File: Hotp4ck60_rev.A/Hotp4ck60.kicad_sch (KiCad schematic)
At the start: 53 parts, among them J1 HRO_TYPE-C-31-M-12, SW44 RST, U1 nRF52840, U2 SRV05-4, Y1 32 MHz, Y2 32.768 Khz

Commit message: Fixed path
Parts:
- removed TP1: TestPoint, TestPoint:TestPoint_THTPad_1.0x1.0mm_Drill0.5mm, symbol Connector:TestPoint
- removed TP2, TP3, TP4: TestPoint, TestPoint:TestPoint_THTPad_D1.0mm_Drill0.5mm, symbol Connector:TestPoint
- added J3, J4: Conn_01x04, Connector_PinSocket_2.54mm:PinSocket_1x04_P2.54mm_Vertical, symbol Connector_Generic:Conn_01x04
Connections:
- net +5V: now also U2.5 (VP), J4.1 (Pin_1); no longer U2.2 (VN)
- net Earth: no longer H1.1
- net GND: now also H1.1, R12.2, R13.2, U2.2 (VN), J3.4 (Pin_4), J4.4 (Pin_4); no longer U2.5 (VP)
- net GNDPWR: no longer R12.2, R13.2
- net SWDCLK: now also J3.3 (Pin_3)
- net SWDIO: now also J3.2 (Pin_2)
- net USB-D+: now also J4.3 (Pin_3)
- net USB-D-: now also J4.2 (Pin_2)
- net VDD: now also J3.1 (Pin_1)
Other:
- moved on the sheet: U2

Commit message: Modified PCB designed
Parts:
- removed C14: 100 nF, Capacitor_SMD:C_0402_1005Metric, symbol Device:C_Small
- removed D64: D_TVS, Diode_SMD:D_SOD-123F, symbol Device:D_TVS
- removed L5 (x2): BLM15PX121SN1D, Inductor_SMD:L_0402_1005Metric, symbol Device:L_Small
- removed R13: 1 MOhm, Resistor_SMD:R_0402_1005Metric, symbol Device:R_Small
- added L5: BLM15PX121SN1D, Inductor_SMD:L_0402_1005Metric, symbol Device:L_Small
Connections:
- net Earth is gone; now on net GND: J1.S1 (SHIELD)
- net GNDPWR is gone; now on net GND: J1.A1 (GND), J1.A12 (GND), J1.B1 (GND), J1.B12 (GND)
- net +5V: no longer U2.5 (VP)
- net VBUS: now also U2.5 (VP), L5.1
- net at F1.1: now also L5.2

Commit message: Modified positions
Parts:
- removed L5: BLM15PX121SN1D, Inductor_SMD:L_0402_1005Metric, symbol Device:L_Small
- J3, J4: now left out of the parts list
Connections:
- net +5V: now also U2.5 (VP)
- net USB-D-: now also U2.4 (IO3); no longer U2.1 (IO1)
- net VBUS: now also F1.1; no longer U2.5 (VP)
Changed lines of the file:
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@@
   (junction (at 27.94 57.15) (diameter 0) (color 0 0 0 0)
   )
-  (junction (at 190.5 104.14) (diameter 0) (color 0 0 0 0)
-  )
   (junction (at 135.89 31.75) (diameter 0.9144) (color 0 0 0 0)
   )
@@
   (junction (at 166.37 93.98) (diameter 0) (color 0 0 0 0)
   )
+  (junction (at 190.5 104.14) (diameter 0) (color 0 0 0 0)
+  )
   (junction (at 72.39 167.64) (diameter 0) (color 0 0 0 0)
   )
@@
   (no_connect (at 102.87 125.73))
   (no_connect (at 102.87 59.69))
-  (no_connect (at 203.2 120.65))
+  (no_connect (at 177.8 115.57))
   (no_connect (at 102.87 77.47))
   (no_connect (at 102.87 105.41))
@@
     (stroke (width 0) (type default))
   )
-  (wire (pts (xy 190.5 104.14) (xy 191.77 104.14))
+  (wire (pts (xy 114.3 34.29) (xy 114.3 35.56))
     (stroke (width 0) (type default))
   )
-  (wire (pts (xy 114.3 34.29) (xy 114.3 35.56))
+  (wire (pts (xy 180.34 104.14) (xy 184.15 104.14))
     (stroke (width 0) (type default))
   )
@@
     (stroke (width 0) (type default))
   )
-  (wire (pts (xy 189.23 104.14) (xy 190.5 104.14))
-    (stroke (width 0) (type solid))
-  )
   (wire (pts (xy 182.88 52.07) (xy 182.88 53.34))
     (stroke (width 0) (type solid))
@@
     (stroke (width 0) (type default))
   )
+  (wire (pts (xy 189.23 104.14) (xy 190.5 104.14))
+    (stroke (width 0) (type default))
+  )
   (wire (pts (xy 165.1 83.82) (xy 168.91 83.82))
     (stroke (width 0) (type solid))
@@
     (stroke (width 0) (type default))
   )
-  (wire (pts (xy 205.74 100.33) (xy 205.74 104.14))
+  (wire (pts (xy 196.85 102.87) (xy 196.85 104.14))
     (stroke (width 0) (type default))
   )
-  (wire (pts (xy 205.74 104.14) (xy 204.47 104.14))
+  (wire (pts (xy 190.5 104.14) (xy 196.85 104.14))
     (stroke (width 0) (type default))
   )
@@
     (stroke (width 0) (type default))
   )
-  (wire (pts (xy 196.85 104.14) (xy 199.39 104.14))
-    (stroke (width 0) (type default))
-  )
   (global_label "DEC1" (shape input) (at 203.2 24.13 90) (fields_autoplaced)
     (effects (font (size 1.27 1.27)) (justify left))
@@
     )
   )
-  (global_label "VBUS" (shape input) (at 189.23 104.14 180) (fields_autoplaced)
+  (global_label "VBUS" (shape input) (at 180.34 104.14 180) (fields_autoplaced)
     (effects (font (size 1.27 1.27)) (justify right))
-    (property "Intersheetrefs" "${INTERSHEET_REFS}" (at 181.4256 104.14 0)
+    (property "Intersheetrefs" "${INTERSHEET_REFS}" (at 172.5356 104.14 0)
       (effects (font (size 1.27 1.27)) (justify right) hide)
     )
@@
     )
   )
-  (global_label "USB-D-" (shape bidirectional) (at 177.8 115.57 180) (fields_autoplaced)
-    (effects (font (size 1.27 1.27)) (justify right))
-    (property "Intersheetrefs" "${INTERSHEET_REFS}" (at 165.5581 115.57 0)
-      (effects (font (size 1.27 1.27)) (justify right) hide)
-    )
-  )
   (global_label "col1" (shape output) (at 102.87 151.13 0) (fields_autoplaced)
     (effects (font (size 1.27 1.27)) (justify left))
@@
     )
   )
+  (global_label "USB-D-" (shape bidirectional) (at 203.2 120.65 0) (fields_autoplaced)
+    (effects (font (size 1.27 1.27)) (justify left))
+    (property "Intersheetrefs" "${INTERSHEET_REFS}" (at 215.4419 120.65 0)
+      (effects (font (size 1.27 1.27)) (justify left) hide)
+    )
+  )
   (global_label "row4" (shape input) (at 102.87 62.23 0) (fields_autoplaced)
     (effects (font (size 1.27 1.27)) (justify left))
@@
     )
   )
+  (symbol (lib_id "Device:Fuse_Small") (at 186.69 104.14 0) (unit 1)
+    (in_bom yes) (on_board yes) (dnp no)
+    (property "Reference" "F1" (at 184.15 101.6 0)
+      (effects (font (size 1.27 1.27)))
+    )
+    (property "Value" "750 mA" (at 190.5 101.6 0)
+      (effects (font (size 1.27 1.27)))
+    )
+    (property "Footprint" "Fuse:Fuse_0603_1608Metric" (at 186.69 104.14 0)
+      (effects (font (size 1.27 1.27)) hide)
+    )
+    (property "Datasheet" "~" (at 186.69 104.14 0)
+      (effects (font (size 1.27 1.27)) hide)
+    )
+    (property "LCSC" "C20792" (at 186.69 104.14 0)
+      (effects (font (size 1.27 1.27)) hide)
+    )
+    (pin "1")
+    (pin "2")
+    (instances
+      (project "osprey_rev_a"
+        (path "/86a516b3-939b-48ee-9a25-d0111c577d06/23ee5603-a56a-413f-b0a5-1709895ff4f1"
+          (reference "F1") (unit 1)
+        )
+      )
+      (project "Hotp4ck60"
+        (path "/a57939d7-40ce-4436-8014-db245ef7f3c5"
+          (reference "F1") (unit 1)
+        )
+      )
+      (project "designguide-schematic"
+        (path "/c2a65ddb-3915-4293-98a9-444287fe2a3d"
+          (reference "F1") (unit 1)
+        )
+      )
+    )
+  )
   (symbol (lib_id "power:+5V") (at 199.39 72.39 0) (unit 1)
     (in_bom yes) (on_board yes) (dnp no)
@@
   )
   (symbol (lib_id "Connector_Generic:Conn_01x04") (at 236.22 40.64 0) (unit 1)
-    (in_bom yes) (on_board yes) (dnp no) (fields_autoplaced)
+    (in_bom no) (on_board yes) (dnp no) (fields_autoplaced)
     (property "Reference" "J3" (at 238.76 40.64 0)
       (effects (font (size 1.27 1.27)) (justify left))
@@
     )
   )
-  (symbol (lib_id "Device:Fuse_Small") (at 201.93 104.14 0) (unit 1)
-    (in_bom yes) (on_board yes) (dnp no)
-    (property "Reference" "F1" (at 199.39 101.6 0)
-      (effects (font (size 1.27 1.27)))
-    )
-    (property "Value" "750 mA" (at 205.74 101.6 0)
-      (effects (font (size 1.27 1.27)))
-    )
-    (property "Footprint" "Fuse:Fuse_0603_1608Metric" (at 201.93 104.14 0)
-      (effects (font (size 1.27 1.27)) hide)
-    )
-    (property "Datasheet" "~" (at 201.93 104.14 0)
-      (effects (font (size 1.27 1.27)) hide)
-    )
-    (property "LCSC" "C20792" (at 201.93 104.14 0)
-      (effects (font (size 1.27 1.27)) hide)
-    )
-    (pin "1")
-    (pin "2")
-    (instances
-      (project "osprey_rev_a"
-        (path "/86a516b3-939b-48ee-9a25-d0111c577d06/23ee5603-a56a-413f-b0a5-1709895ff4f1"
-          (reference "F1") (unit 1)
-        )
-      )
-      (project "Hotp4ck60"
-        (path "/a57939d7-40ce-4436-8014-db245ef7f3c5"
-          (reference "F1") (unit 1)
-        )
-      )
-      (project "designguide-schematic"
-        (path "/c2a65ddb-3915-4293-98a9-444287fe2a3d"
-          (reference "F1") (unit 1)
-        )
-      )
-    )
-  )
   (symbol (lib_id "PCM_marbastlib-various:SRV05-4") (at 190.5 118.11 0) (unit 1)
     (in_bom yes) (on_board yes) (dnp no)
@@
     )
   )
-  (symbol (lib_id "Device:L_Small") (at 194.31 104.14 90) (unit 1)
-    (in_bom yes) (on_board yes) (dnp no)
-    (property "Reference" "L5" (at 194.31 101.6 90)
-      (effects (font (size 1.27 1.27)))
-    )
-    (property "Value" "BLM15PX121SN1D" (at 194.31 106.68 90)
-      (effects (font (size 1.27 1.27)))
-    )
-    (property "Footprint" "Inductor_SMD:L_0402_1005Metric" (at 194.31 104.14 0)
-      (effects (font (size 1.27 1.27)) hide)
-    )
-    (property "Datasheet" "~" (at 194.31 104.14 0)
-      (effects (font (size 1.27 1.27)) hide)
-    )
-    (property "LCSC" "C88970" (at 194.31 104.14 90)
-      (effects (font (size 1.27 1.27)) hide)
-    )
-    (pin "1")
-    (pin "2")
-    (instances
-      (project "osprey_rev_a"
-        (path "/86a516b3-939b-48ee-9a25-d0111c577d06/23ee5603-a56a-413f-b0a5-1709895ff4f1"
-          (reference "L5") (unit 1)
-        )
-      )
-      (project "Hotp4ck60"
-        (path "/a57939d7-40ce-4436-8014-db245ef7f3c5"
-          (reference "L5") (unit 1)
-        )
-      )
-      (project "designguide-schematic"
-        (path "/c2a65ddb-3915-4293-98a9-444287fe2a3d"
-          (reference "L6") (unit 1)
-        )
-      )
-    )
-  )
   (symbol (lib_id "Device:C_Small") (at 168.91 29.21 0) (unit 1)
     (in_bom yes) (on_board yes) (dnp no)
@@
   )
   (symbol (lib_id "Connector_Generic:Conn_01x04") (at 208.28 74.93 0) (unit 1)
-    (in_bom yes) (on_board yes) (dnp no)
+    (in_bom no) (on_board yes) (dnp no)
     (property "Reference" "J4" (at 207.01 82.55 0)
       (effects (font (size 1.27 1.27)) (justify left))
@@
     )
   )
-  (symbol (lib_id "power:+5V") (at 205.74 100.33 0) (unit 1)
+  (symbol (lib_id "power:+5V") (at 196.85 102.87 0) (unit 1)
     (in_bom yes) (on_board yes) (dnp no)
-    (property "Reference" "#PWR029" (at 205.74 104.14 0)
+    (property "Reference" "#PWR029" (at 196.85 106.68 0)
       (effects (font (size 1.27 1.27)) hide)
     )
-    (property "Value" "+5V" (at 208.28 99.06 0)
+    (property "Value" "+5V" (at 199.39 101.6 0)
       (effects (font (size 1.27 1.27)))
     )
-    (property "Footprint" "" (at 205.74 100.33 0)
+    (property "Footprint" "" (at 196.85 102.87 0)
       (effects (font (size 1.27 1.27)) hide)
     )
-    (property "Datasheet" "" (at 205.74 100.33 0)
+    (property "Datasheet" "" (at 196.85 102.87 0)
       (effects (font (size 1.27 1.27)) hide)
     )

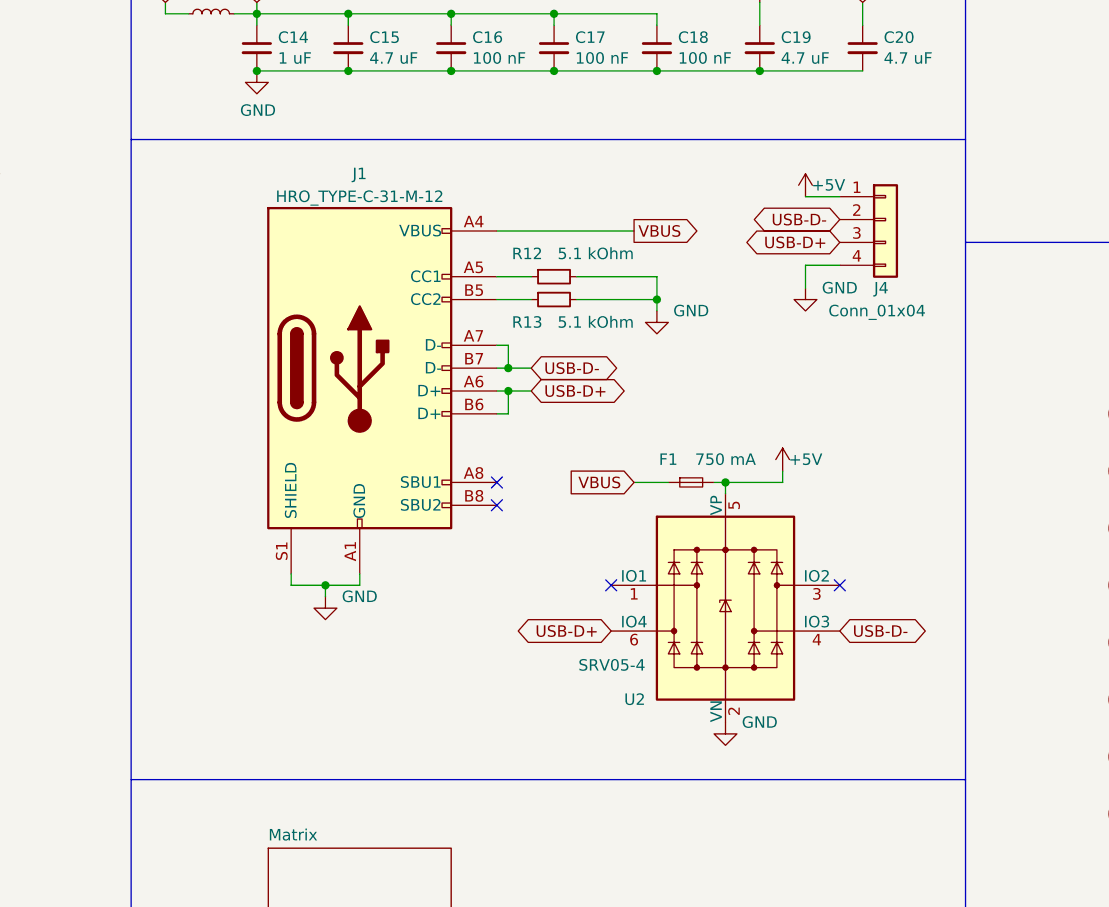
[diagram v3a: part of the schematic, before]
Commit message: unified daughterboard, MCU 추가
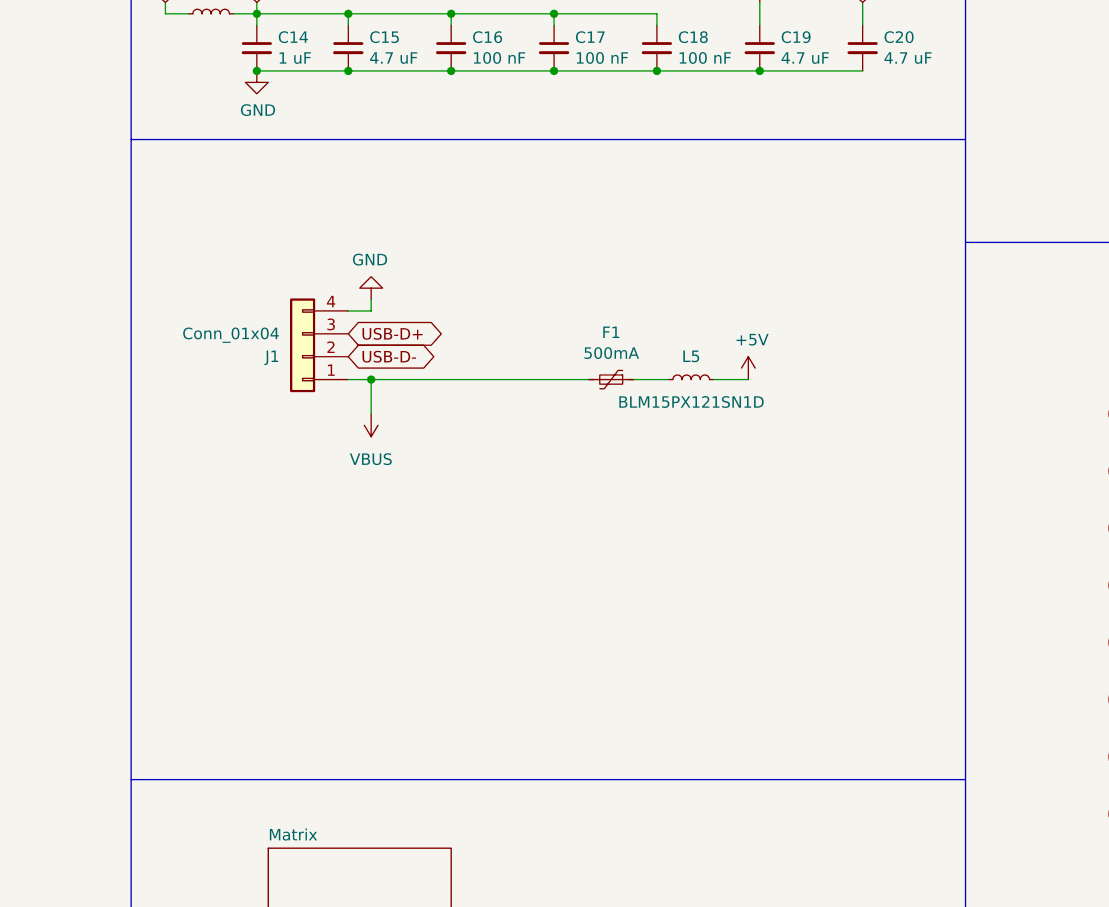
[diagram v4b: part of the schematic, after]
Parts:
- removed F1: 750 mA, Fuse:Fuse_0603_1608Metric, symbol Device:Fuse_Small
- removed J1: HRO_TYPE-C-31-M-12, Connector_USB:USB_C_Receptacle_HRO_TYPE-C-31-M-12, symbol Connector:USB_C_Receptacle_USB2.0
- removed J4: Conn_01x04, Connector_PinSocket_2.54mm:PinSocket_1x04_P2.54mm_Vertical, symbol Connector_Generic:Conn_01x04
- removed R12, R13: 5.1 kOhm, Resistor_SMD:R_0402_1005Metric, symbol Device:R_Small
- removed U2: SRV05-4, PCM_marbastlib-various:SOT-23-6-routable, symbol PCM_marbastlib-various:SRV05-4
- added F1: 500mA, Fuse:Fuse_0603_1608Metric, symbol Device:Polyfuse_Small
- added J1: Conn_01x04, Connector_JST:JST_SH_SM04B-SRSS-TB_1x04-1MP_P1.00mm_Horizontal, symbol Connector_Generic:Conn_01x04
- added L5: BLM15PX121SN1D, Inductor_SMD:L_0402_1005Metric, symbol Device:L_Small
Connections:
- net +5V: now also L5.2
- net GND: now also J1.4 (Pin_4)
- net USB-D+: now also J1.3 (Pin_3)
- net USB-D-: now also J1.2 (Pin_2)
- net VBUS: now also F1.2, J1.1 (Pin_1)
- new net: F1.1, L5.1
- no-connect marks 26 -> 22

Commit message: 리비젼A 수정
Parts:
- removed H1: MountingHole, amtra5_outline:60_Outline-Modded-Type-C, symbol Mechanical:MountingHole
- removed J1: Conn_01x04, Connector_JST:JST_SH_SM04B-SRSS-TB_1x04-1MP_P1.00mm_Horizontal, symbol Connector_Generic:Conn_01x04
- removed L5: BLM15PX121SN1D, Inductor_SMD:L_0402_1005Metric, symbol Device:L_Small
- added H8: MountingHole, Hotp4ck:Neo60_2, symbol Mechanical:MountingHole
- added J1: Conn_01x05_Pin, Connector_PinHeader_2.54mm:PinHeader_1x05_P2.54mm_Vertical, symbol Connector:Conn_01x05_Pin
- renumbered C3 to C1, C9 to C10, C4 to C2, C5 to C3, C1 to C6, C2 to C7, C10 to C8, C8 to C9, H2 to H1, R3 to R5, SW44 to SW1
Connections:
- net +5V: now also F1.2
- net GND: now also J1.4 (Pin_4)
- net USB-D+: now also J1.3 (Pin_3)
- net USB-D-: now also J1.2 (Pin_2)
- net VBUS: now also F1.1, J1.1 (Pin_1); no longer F1.2
- net col0: now also U1.B13 (AIN1/P0.03); no longer U1.A12 (AIN0/P0.02)
- net col10: now also U1.L24 (NFC1/P0.09); no longer U1.R24 (P1.06)
- net col11: now also U1.R24 (P1.06); no longer U1.U24 (P1.04)
- net col12: now also U1.U24 (P1.04); no longer U1.W24 (P1.02)
- net col13: now also U1.W24 (P1.02); no longer U1.AC21 (P0.25), U1.AD22 (TRACEDATA0/P1.00)
- net col2: now also U1.B15 (P1.14); no longer U1.A16 (P1.13)
- net col3: now also U1.A16 (P1.13); no longer U1.A20 (P1.10)
- net col4: now also U1.A12 (AIN0/P0.02); no longer U1.J1 (AIN2/P0.04)
- net col5: now also U1.A10 (AIN5/P0.29); no longer U1.AD16 (P0.20)
- net col6: now also U1.A20 (P1.10); no longer U1.J24 (NFC2/P0.10)
- net col7: now also U1.J1 (AIN2/P0.04); no longer U1.AD18 (P0.22)
- net col8: now also U1.J24 (NFC2/P0.10); no longer U1.L24 (NFC1/P0.09)
- net row3: now also U1.G1 (P0.26); no longer U1.A10 (AIN5/P0.29)
- new net +BATT: J1.5 (Pin_5)
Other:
- moved on the sheet: F1

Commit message: 배선 완료
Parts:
- removed C1: NC, Capacitor_SMD:C_0402_1005Metric, symbol Device:C_Small
- removed J3: Conn_01x04, Connector_PinSocket_2.54mm:PinSocket_1x04_P2.54mm_Vertical, symbol Connector_Generic:Conn_01x04
- removed LED1: Blue, LED_SMD:LED_0603_1608Metric, symbol Device:LED_Small
- removed SW1: RST, marbastlib-various:SW_SPST_SKQG_WithStem, symbol Switch:SW_SPST
- added J2: Conn_01x05_Socket, Connector_PinSocket_2.54mm:PinSocket_1x05_P2.54mm_Vertical, symbol Connector:Conn_01x05_Socket
- added L2: 4.7 nH, Inductor_SMD:L_0402_1005Metric, symbol Device:L_Small
- added LED1: LED_MHT151RGBCT, PCM_marbastlib-various:LED_1206R, symbol PCM_marbastlib-choc:choc_MHT151RGBCT
- added R10, R9: 1k, Resistor_SMD:R_0402_1005Metric, symbol Device:R_Small
- added U3: SRV05-4, PCM_marbastlib-various:SOT-23-6-routable, symbol PCM_marbastlib-various:SRV05-4
- C1: renamed from C2; value 0.5 pF -> 1.2 pF; LCSC C77179 -> C327292; Notes NP0, 10% -> (none)
- C2: renamed from C3; value 0.8 pF -> 1 pF; LCSC C285068 -> C309455; Notes NP0, 10% -> (none)
- C3: renamed from C4; LCSC (none) -> C1547
- C4: renamed from C5; LCSC (none) -> C1547
- J1: now left out of the parts list
- R8: renamed from R5; value 1 kOhm -> 1k
- U1: LCSC (none) -> C190794
- Y1: LCSC (none) -> C2149125
- Y2: LCSC (none) -> C55208
- renumbered C6 to C5, C7 to C6, L2 to L3, L3 to L4, L4 to L5
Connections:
- net GND: now also J2.4 (Pin_4), U3.2 (VN)
- net RST: now also J2.5 (Pin_5)
- net SWDCLK: now also J2.3 (Pin_3)
- net SWDIO: now also J2.2 (Pin_2)
- net USB-D+: now also U3.1 (IO1)
- net USB-D-: now also U3.6 (IO4)
- net VBUS: now also U3.5 (VP)
- net VDD: now also J2.1 (Pin_1), LED1.1 (A)
- net col4: now also U1.A10 (AIN5/P0.29); no longer U1.A12 (AIN0/P0.02)
- net col5: now also U1.A8 (AIN7/P0.31); no longer U1.A10 (AIN5/P0.29)
- net col9: now also U1.AD16 (P0.20); no longer U1.AD20 (P0.24)
- net at C1.2, L1.1: now also L2.2; no longer AE1.1
- net LED_B: now reaches R8.2
- net LED_B: now also U1.A12 (AIN0/P0.02)
- net LED: no longer names the net of R8.1
- net LED: now also LED1.2 (BK); no longer U1.A8 (AIN7/P0.31)
- new net: LED1.3 (GK), R9.1
- new net: LED1.4 (RK), R10.1
- new net: AE1.1, L2.1
- new net LED_G: R9.2
- new net ~{CHG}: R10.2
- no-connect marks 22 -> 24
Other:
- moved on the sheet: F1, J1, R8
